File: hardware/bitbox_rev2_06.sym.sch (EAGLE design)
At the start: 65 parts, among them IC3 LM317MSTT3, Q1 8MHz, U1 USD-SOCKETNEW, X2 2510-

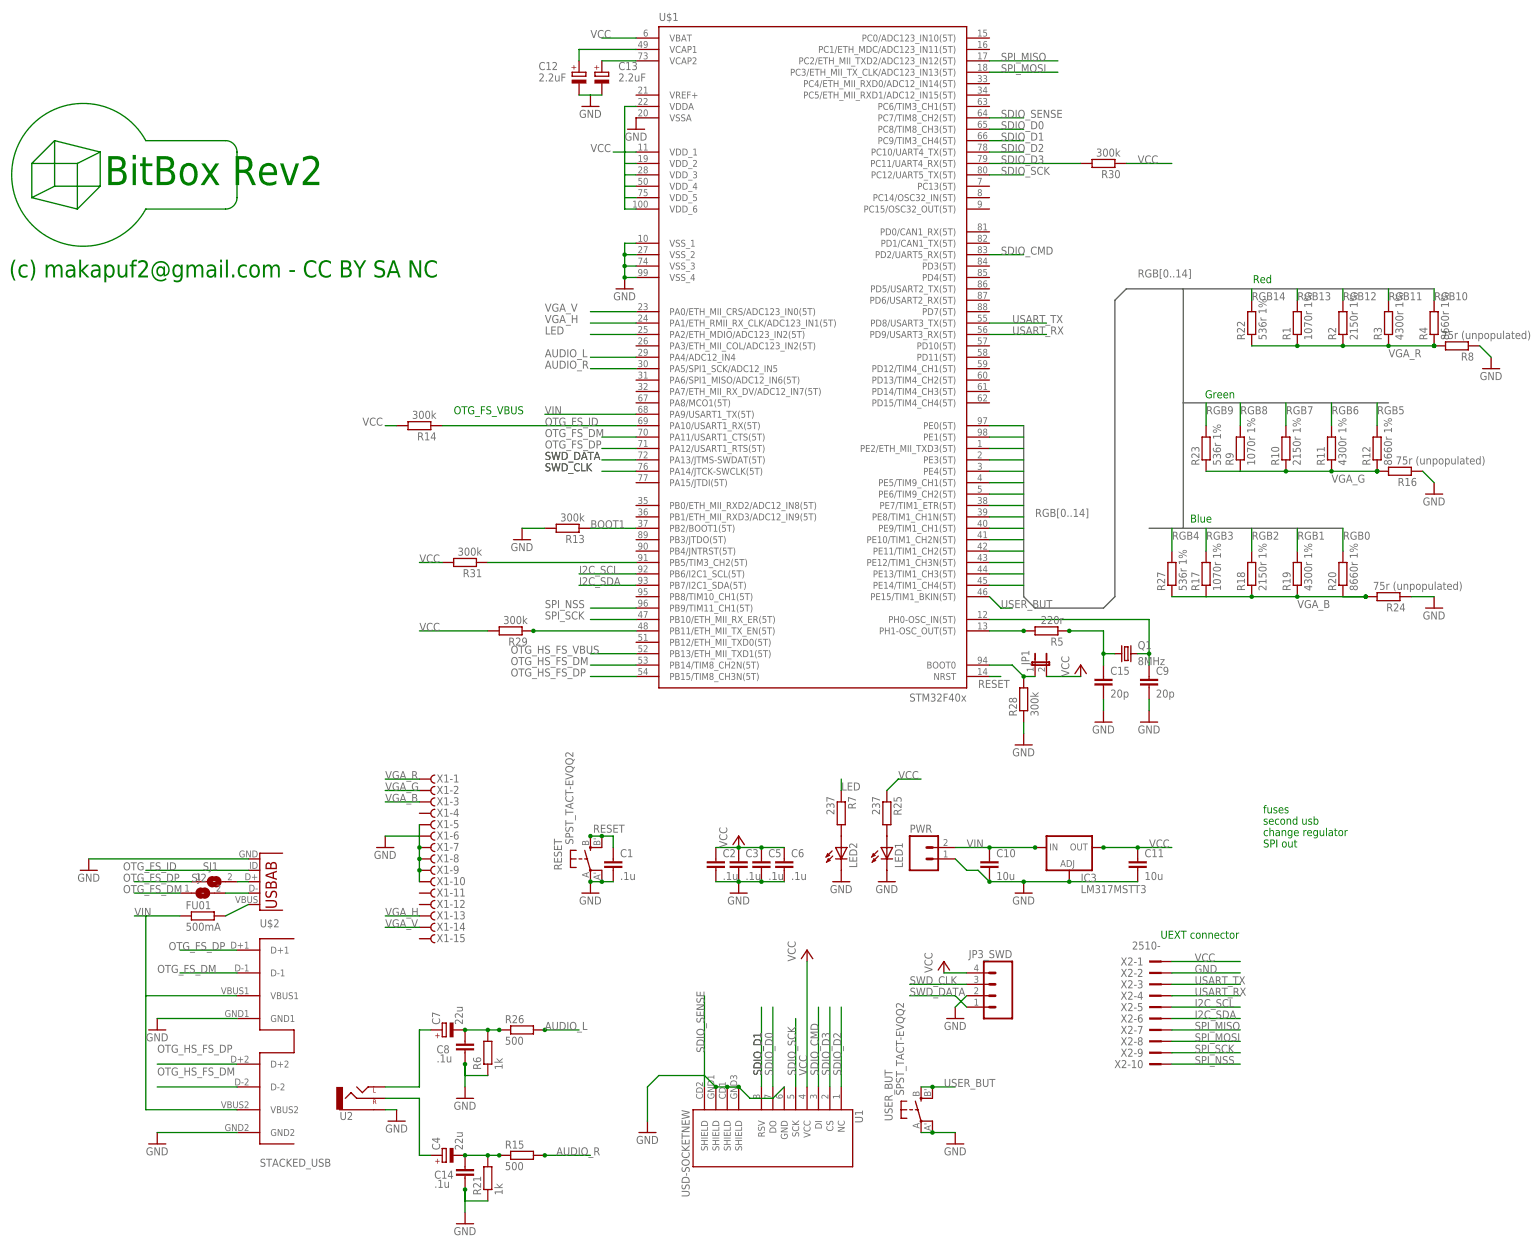
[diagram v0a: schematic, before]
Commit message: updated board, added component values
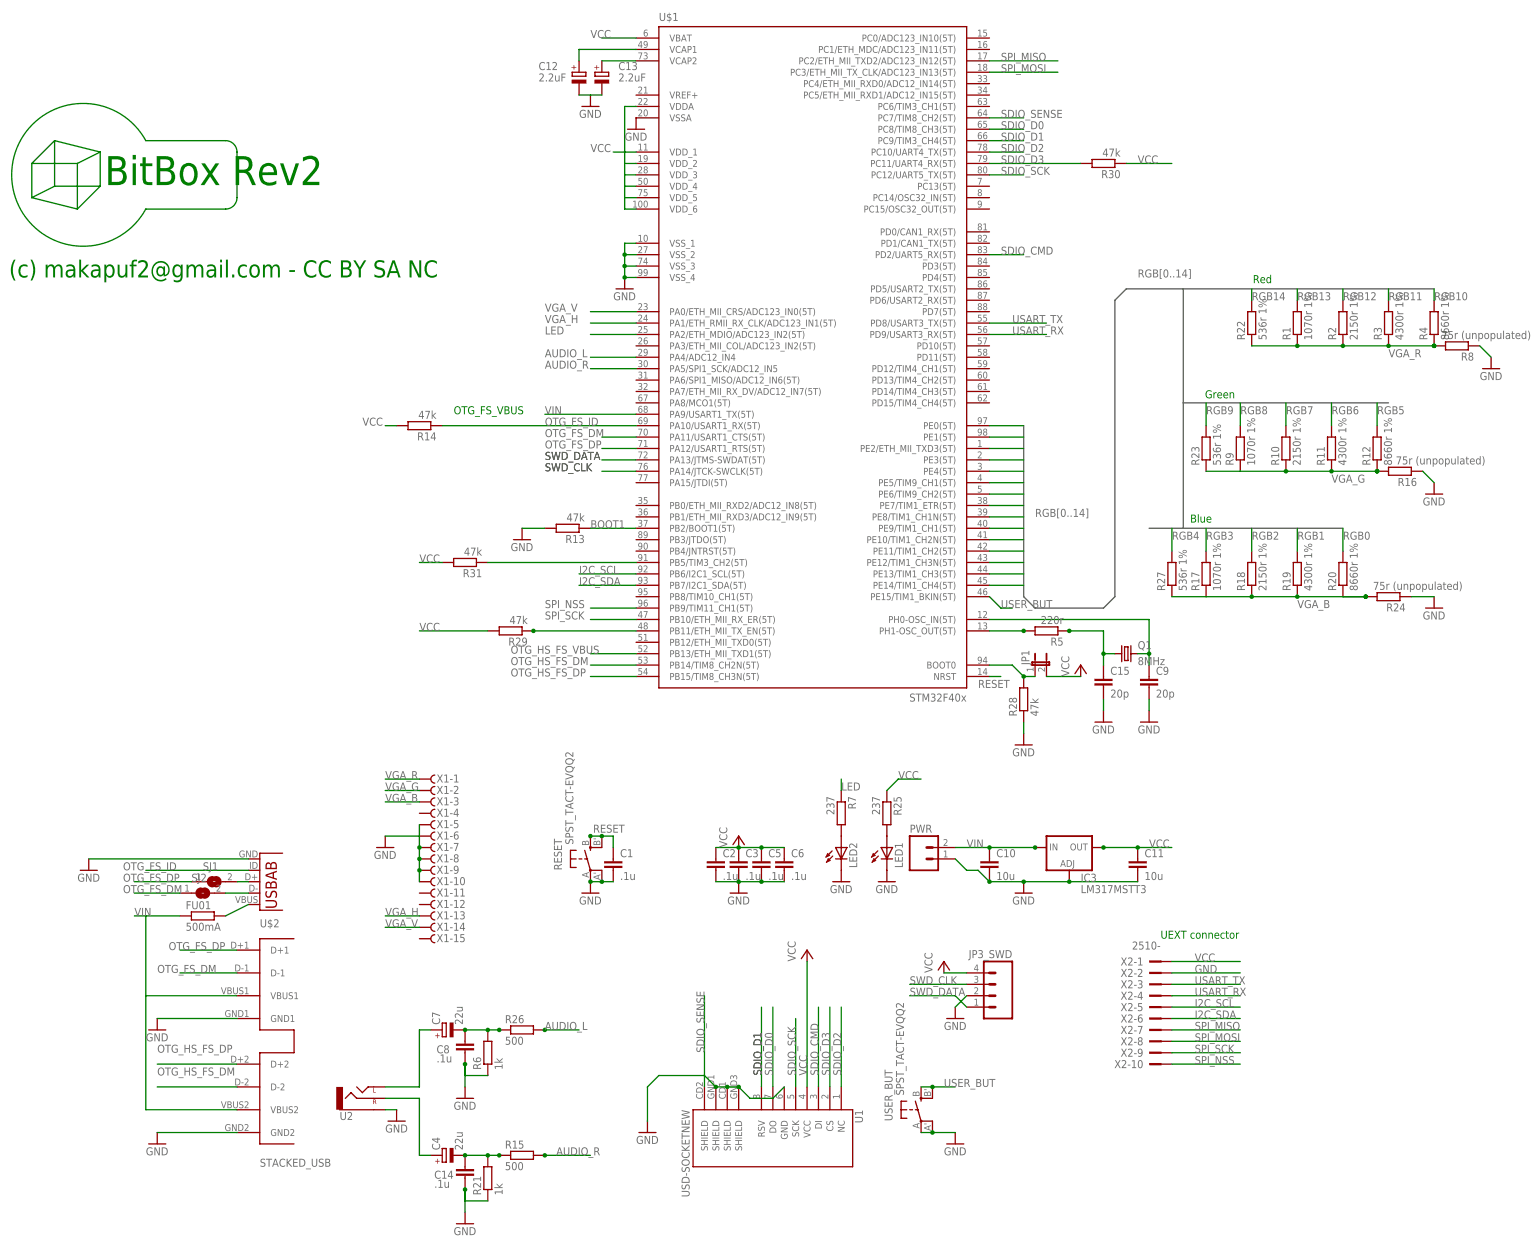
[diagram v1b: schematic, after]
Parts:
- R13, R14, R28, R29, R30, R31: value 300k -> 47k
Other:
- note removed: "SPI out"
- note removed: "change regulator"
- note removed: "fuses"
- note removed: "second usb"
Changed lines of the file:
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@@
 <part name="GND20" library="supply1" deviceset="GND" device=""/>
 <part name="GND26" library="supply1" deviceset="GND" device=""/>
-<part name="R28" library="resistor" deviceset="R-EU_" device="R0603" value="300k"/>
+<part name="R28" library="resistor" deviceset="R-EU_" device="R0603" value="47k"/>
 <part name="GND22" library="supply1" deviceset="GND" device=""/>
 <part name="P+7" library="supply1" deviceset="VCC" device=""/>
@@
 <part name="X2" library="con-3m" deviceset="2510-" device=""/>
 <part name="C1" library="resistor" deviceset="C-EU" device="C0603" value=".1u"/>
-<part name="R13" library="resistor" deviceset="R-EU_" device="R0603" value="300k"/>
+<part name="R13" library="resistor" deviceset="R-EU_" device="R0603" value="47k"/>
 <part name="GND6" library="supply1" deviceset="GND" device=""/>
 <part name="P+3" library="supply1" deviceset="VCC" device=""/>
 <part name="JP1" library="jumper" deviceset="JP1E" device=""/>
 <part name="GND8" library="supply1" deviceset="GND" device=""/>
-<part name="R14" library="resistor" deviceset="R-EU_" device="R0603" value="300k"/>
-<part name="R29" library="resistor" deviceset="R-EU_" device="R0603" value="300k"/>
-<part name="R30" library="resistor" deviceset="R-EU_" device="R0603" value="300k"/>
-<part name="R31" library="resistor" deviceset="R-EU_" device="R0603" value="300k"/>
+<part name="R14" library="resistor" deviceset="R-EU_" device="R0603" value="47k"/>
+<part name="R29" library="resistor" deviceset="R-EU_" device="R0603" value="47k"/>
+<part name="R30" library="resistor" deviceset="R-EU_" device="R0603" value="47k"/>
+<part name="R31" library="resistor" deviceset="R-EU_" device="R0603" value="47k"/>
 </parts>
 <sheets>
@@
 <text x="157.226" y="206.756" size="1.778" layer="91">Green</text>
 <text x="153.924" y="179.07" size="1.778" layer="91">Blue</text>
-<text x="170.18" y="114.3" size="1.778" layer="91">fuses</text>
-<text x="170.18" y="111.76" size="1.778" layer="91">second usb</text>
-<text x="170.18" y="109.22" size="1.778" layer="91">change regulator</text>
-<text x="170.18" y="106.68" size="1.778" layer="91">SPI out</text>
 <text x="147.32" y="86.36" size="1.778" layer="91">UEXT connector</text>
 <text x="-10.16" y="203.2" size="1.778" layer="91">OTG_FS_VBUS</text>
